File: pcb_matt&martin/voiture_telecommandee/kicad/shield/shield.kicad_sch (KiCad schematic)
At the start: 13 parts, among them J2 Bluetooth, U1 COM-09032

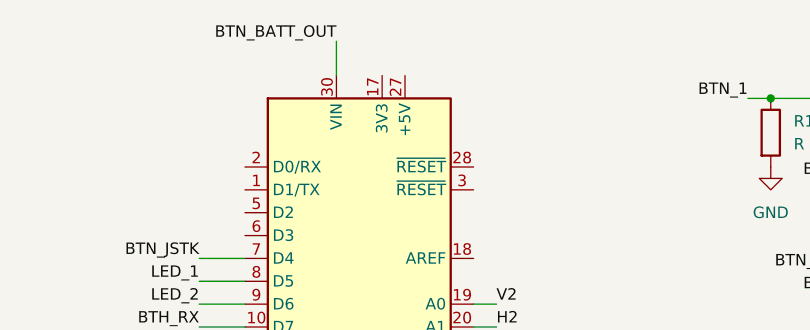
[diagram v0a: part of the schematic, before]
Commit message: Résolu Issue #12
J'ai tout simplement mis le symbole sur l'Arduino et rerouté et tout le tralala
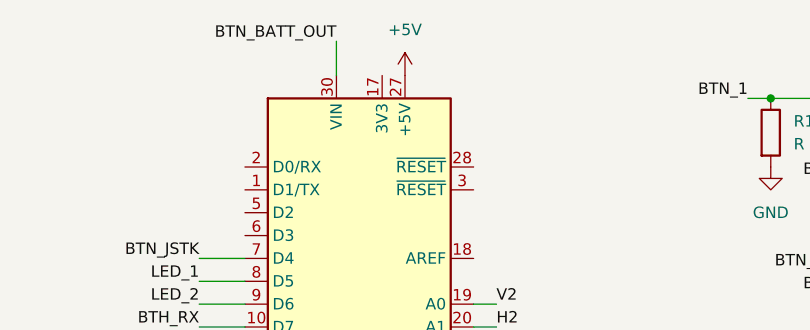
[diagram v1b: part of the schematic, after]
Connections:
- net +5V: now also A1.27 (+5V)
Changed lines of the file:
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@@
+	)
+	(symbol
+		(lib_id "power:+5V")
+		(at 149.86 74.93 0)
+		(unit 1)
+		(exclude_from_sim no)
+		(in_bom yes)
+		(on_board yes)
+		(dnp no)
+		(fields_autoplaced yes)
+		(property "Reference" "#PWR020"
+			(at 149.86 78.74 0)
+			(effects
+				(font
+					(size 1.27 1.27)
+				)
+				(hide yes)
+			)
+		)
+		(property "Value" "+5V"
+			(at 149.86 69.85 0)
+			(effects
+				(font
+					(size 1.27 1.27)
+				)
+			)
+		)
+		(property "Footprint" ""
+			(at 149.86 74.93 0)
+			(effects
+				(font
+					(size 1.27 1.27)
+				)
+				(hide yes)
+			)
+		)
+		(property "Datasheet" ""
+			(at 149.86 74.93 0)
+			(effects
+				(font
+					(size 1.27 1.27)
+				)
+				(hide yes)
+			)
+		)
+		(property "Description" "Power symbol creates a global label with name \"+5V\""
+			(at 149.86 74.93 0)
+			(effects
+				(font
+					(size 1.27 1.27)
+				)
+				(hide yes)
+			)
+		)
+		(pin "1"
+		)
+		(instances
+			(project ""
+				(path "/a3b22e48-2c1e-4c6b-b8ab-3c8951b024b5"
+					(reference "#PWR020")
+					(unit 1)
+				)
+			)
+		)
 	)
 	(symbol

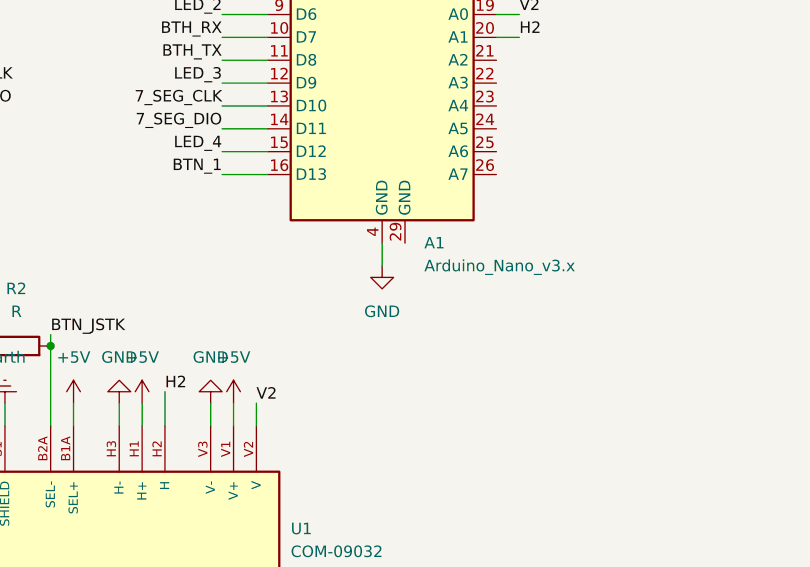
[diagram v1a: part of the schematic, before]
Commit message: Résolution de l'issue #11
Pas sûr-sûr que fallait faire comme ça mais bon (https://github.com/Y159753/v-rification_pcb_manette_les_experts/issues/11#issuecomment-3921551236) Donc du coup j'ai mis le signe gnd sur la 2eme broche gnd de l'Arduino.
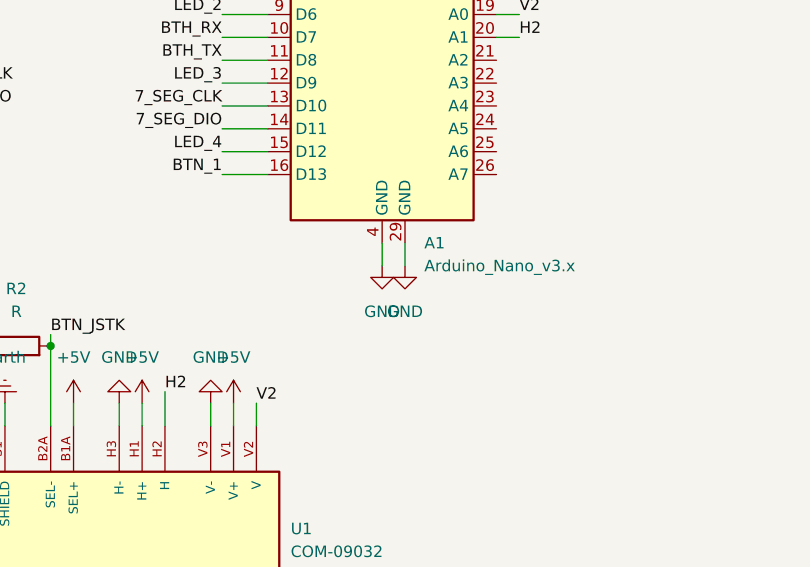
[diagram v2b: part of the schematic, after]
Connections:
- net GND: now also A1.29 (GND)
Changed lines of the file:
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@@
+	(wire
+		(pts
+			(xy 147.32 125.73) (xy 147.32 128.27)
+		)
+		(stroke
+			(width 0)
+			(type default)
+		)
+	)
 	(wire
 		(pts
@@
 					(unit 1)
 				)
+			)
+		)
+	)
+	(symbol
+		(lib_id "power:GND")
+		(at 147.32 128.27 0)
+		(unit 1)
+		(exclude_from_sim no)
+		(in_bom yes)
+		(on_board yes)
+		(dnp no)
+		(fields_autoplaced yes)
+		(property "Reference" "#PWR021"
+			(at 147.32 134.62 0)
+			(effects
+				(font
+					(size 1.27 1.27)
+				)
+				(hide yes)
+			)
+		)
+		(property "Value" "GND"
+			(at 147.32 133.35 0)
+			(effects
+				(font
+					(size 1.27 1.27)
+				)
+			)
+		)
+		(property "Footprint" ""
+			(at 147.32 128.27 0)
+			(effects
+				(font
+					(size 1.27 1.27)
+				)
+				(hide yes)
+			)
+		)
+		(property "Datasheet" ""
+			(at 147.32 128.27 0)
+			(effects
+				(font
+					(size 1.27 1.27)
+				)
+				(hide yes)
+			)
+		)
+		(property "Description" "Power symbol creates a global label with name \"GND\" , ground"
+			(at 147.32 128.27 0)
+			(effects
+				(font
+					(size 1.27 1.27)
+				)
+				(hide yes)
+			)
+		)
+		(pin "1"
+		)
+		(instances
+			(project ""
+				(path "/a3b22e48-2c1e-4c6b-b8ab-3c8951b024b5"
+					(reference "#PWR021")
+					(unit 1)
+				)

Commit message: bon euuuuu y'a bcp de changements
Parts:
- renumbered A1 to ARDUINO1, J2 to Bluetooth1, Bouton_1 to Bouton1, Bouton_d'alimentation1 to Btn_alim1, U1 to Joystick1, D1 to LED1, D2 to LED2, D3 to LED3, D4 to LED4
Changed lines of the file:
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@@
 		(on_board yes)
 		(dnp no)
-		(fields_autoplaced yes)
-		(property "Reference" "D1"
+		(property "Reference" "LED1"
 			(at 210.5025 105.41 0)
 			(effects
@@
 					(size 1.27 1.27)
 				)
+				(hide yes)
 			)
 		)
@@
 			(project ""
 				(path "/a3b22e48-2c1e-4c6b-b8ab-3c8951b024b5"
-					(reference "D1")
+					(reference "LED1")
 					(unit 1)
 				)
@@
 		(dnp no)
 		(fields_autoplaced yes)
-		(property "Reference" "A1"
+		(property "Reference" "ARDUINO1"
 			(at 149.4633 125.73 0)
 			(effects
@@
 			(project ""
 				(path "/a3b22e48-2c1e-4c6b-b8ab-3c8951b024b5"
-					(reference "A1")
+					(reference "ARDUINO1")
 					(unit 1)
 				)
@@
 		(on_board yes)
 		(dnp no)
-		(property "Reference" "J2"
+		(property "Reference" "Bluetooth1"
 			(at 69.85 76.1999 0)
 			(effects
@@
 			(project ""
 				(path "/a3b22e48-2c1e-4c6b-b8ab-3c8951b024b5"
-					(reference "J2")
+					(reference "Bluetooth1")
 					(unit 1)
 				)
@@
 		(dnp no)
 		(fields_autoplaced yes)
-		(property "Reference" "Bouton_1"
+		(property "Reference" "Bouton1"
 			(at 215.9 74.9299 0)
 			(effects
@@
 			(project ""
 				(path "/a3b22e48-2c1e-4c6b-b8ab-3c8951b024b5"
-					(reference "Bouton_1")
+					(reference "Bouton1")
 					(unit 1)
 				)
@@
 		(dnp no)
 		(fields_autoplaced yes)
-		(property "Reference" "Bouton_d'alimentation1"
+		(property "Reference" "Btn_alim1"
 			(at 214.63 96.5199 0)
 			(effects
@@
 			(project ""
 				(path "/a3b22e48-2c1e-4c6b-b8ab-3c8951b024b5"
-					(reference "Bouton_d'alimentation1")
+					(reference "Btn_alim1")
 					(unit 1)
 				)
@@
 		(dnp no)
 		(fields_autoplaced yes)
-		(property "Reference" "D2"
+		(property "Reference" "LED2"
 			(at 210.5025 111.76 0)
 			(effects
@@
 					(size 1.27 1.27)
 				)
+				(hide yes)
 			)
 		)
@@
 			(project "shield"
 				(path "/a3b22e48-2c1e-4c6b-b8ab-3c8951b024b5"
-					(reference "D2")
+					(reference "LED2")
 					(unit 1)
 				)
@@
 		(dnp no)
 		(fields_autoplaced yes)
-		(property "Reference" "U1"
+		(property "Reference" "Joystick1"
 			(at 134.62 157.4799 90)
 			(effects
@@
 			(project ""
 				(path "/a3b22e48-2c1e-4c6b-b8ab-3c8951b024b5"
-					(reference "U1")
+					(reference "Joystick1")
 					(unit 1)
 				)
@@
 		(dnp no)
 		(fields_autoplaced yes)
-		(property "Reference" "D4"
+		(property "Reference" "LED4"
 			(at 210.5025 124.46 0)
 			(effects
@@
 					(size 1.27 1.27)
 				)
+				(hide yes)
 			)
 		)
@@
 			(project "shield"
 				(path "/a3b22e48-2c1e-4c6b-b8ab-3c8951b024b5"
-					(reference "D4")
+					(reference "LED4")
 					(unit 1)
 				)
@@
 		(dnp no)
 		(fields_autoplaced yes)
-		(property "Reference" "D3"
+		(property "Reference" "LED3"
 			(at 210.5025 118.11 0)
 			(effects
@@
 					(size 1.27 1.27)
 				)
+				(hide yes)
 			)
 		)
@@
 			(project "shield"
 				(path "/a3b22e48-2c1e-4c6b-b8ab-3c8951b024b5"
-					(reference "D3")
-					(unit 1)
-				)
+					(reference "LED3")
+					(unit 1)
+				)
